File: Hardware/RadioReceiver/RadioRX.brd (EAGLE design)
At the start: 100 x 80 mm, 49 parts, among them IC1 7805TV, Q1 BSS123, Q10 BSS123, Q11 BSS123, Q12 BSS123, Q13 BSS123, Q14 BSS123, Q2 BSS123, Q3 BSS84, Q4 BSS84, Q5 BSS84, Q6 BSS84, Q7 BSS123, Q8 BSS123, Q9 BSS123

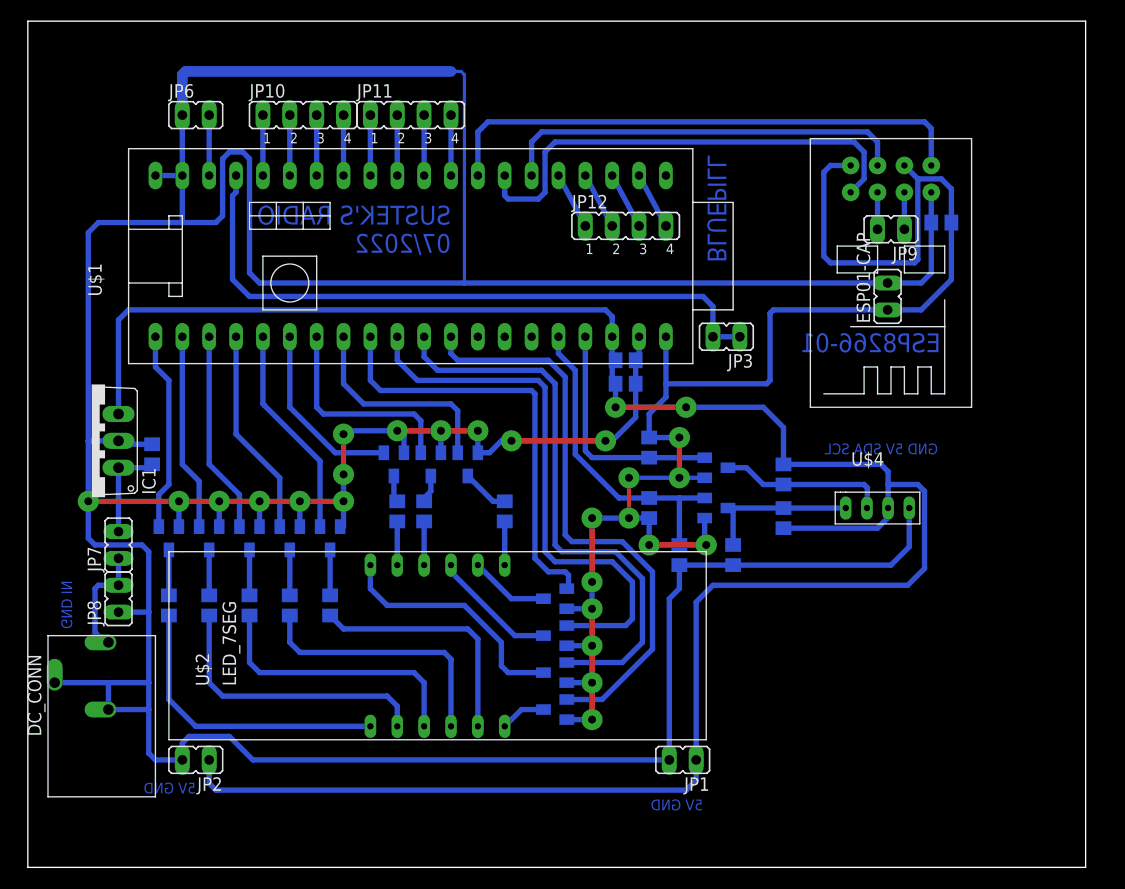
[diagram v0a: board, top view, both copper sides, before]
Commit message: Cleaned HW, prepared for NCODER, time (slows 1minute/hours)
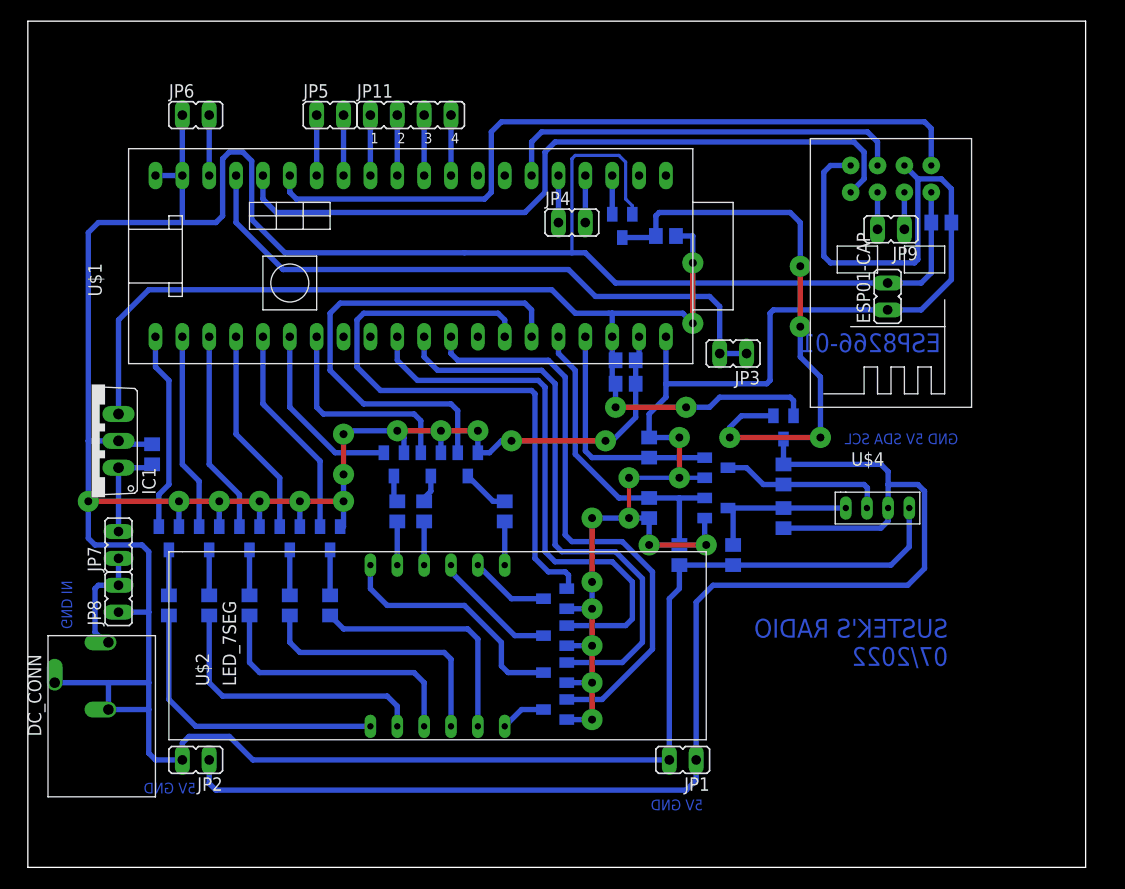
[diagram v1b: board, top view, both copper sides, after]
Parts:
- removed JP10, JP12: (no value), jumper:JP4
- added JP4, JP5: (no value), jumper:JP1
- added Q15: BSS123, transistor-small-signal:SOT23
- added Q17: BSS84, transistor-small-signal:SOT23
- added R13: 10k, rcl:R0805
- moved JP3 1.71 mm to (66.7, 48.6)
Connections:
- net N$10 renamed EE_NCS
- net N$7 renamed EE_MOSI
- net N$8 renamed EE_MISO
- net N$9 renamed EE_SCK
- removed net N$13: JP12.3, U$1.P$23
- removed net N$14: JP12.4, U$1.P$22
- removed net N$3: JP10.1, U$1.P$36
- removed net N$4: JP10.2, U$1.P$35
- removed net N$5: JP10.3, U$1.P$34
- removed net N$6: JP10.4, U$1.P$33
- new net 5V_S: JP1.1, JP2.1, Q17.3, R3.2, R4.2, U$4.P$3
- new net EE_GND: JP5.1, U$1.P$34
- new net EE_VCC: JP5.2, U$1.P$33
- new net N$15: Q15.3, Q17.1, R13.1
- new net RDA_SWITCH_PWR: Q15.1, U$1.P$23
- net 5V: now also Q17.2, R13.2; no longer JP1.1, JP2.1, R3.2, R4.2, U$4.P$3
- net ESP-RX: now also U$1.P$36; no longer U$1.P$27
- net ESP-TX: now also U$1.P$35; no longer U$1.P$28
- net GND: now also Q15.2
- net LEDC_A3: now also U$1.P$14; no longer U$1.P$9
- net LEDC_B: now also U$1.P$15; no longer U$1.P$8
- net N$11: now also JP4.1; no longer JP12.1
- net N$12: now also JP4.2; no longer JP12.2
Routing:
- net 5V_S: track 0.00 -> 127.1 mm
- net 5V: track 210.0 -> 103.8 mm, vias 2 -> 4
- net N$15: track 0.00 -> 54.6 mm, vias 0 -> 4
- net GND: track 430.4 -> 396.4 mm
- net LEDC_B: track 20.3 -> 45.3 mm
- net ESP-RX: track 45.2 -> 69.3 mm
- net ESP-TX: track 51.1 -> 72.6 mm
- net LEDC_A3: track 40.9 -> 59.1 mm
- net N$6: track 5.72 -> 0.00 mm
- net N$5: track 5.72 -> 0.00 mm
- net N$4: track 5.72 -> 0.00 mm
- net N$3: track 5.72 -> 0.00 mm
- net EE_VCC: track 0.00 -> 5.72 mm
- net EE_GND: track 0.00 -> 5.72 mm
- net N$14: track 5.40 -> 0.00 mm
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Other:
- board text removed: "BLUEPILL"

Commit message: Almost final state, just a 32.768 XTAL misses to be soldered
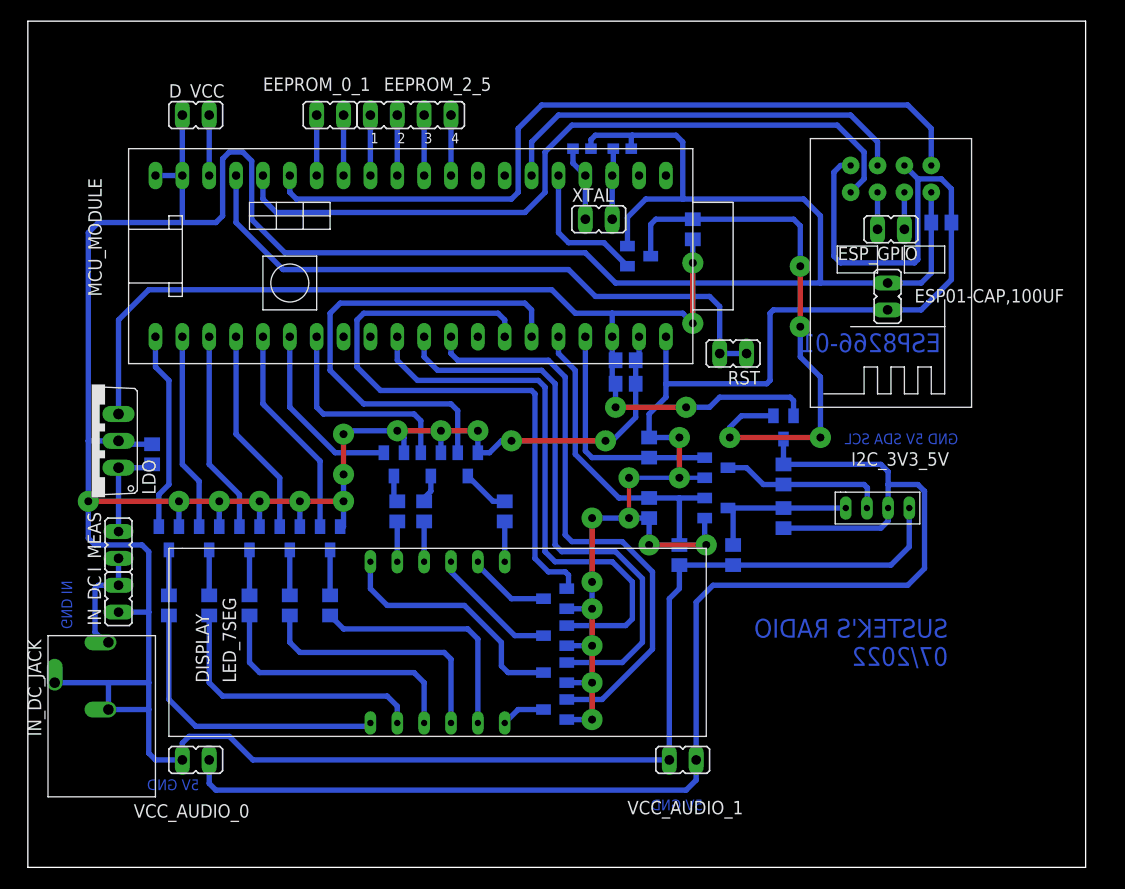
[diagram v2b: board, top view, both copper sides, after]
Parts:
- removed JP4: (no value), jumper:JP1
- removed U$2: LED_7SEG, VladimirSustek:LED_7SEG
- added C7, C8: 12p, rcl:C0603
- added DISPLAY: LED_7SEG, VladimirSustek:LED_7SEG
- added XTAL: (no value), jumper:JP1
- C1, C2: value (none) -> DNI 100p
- C3, C5, C6: value (none) -> 100n
- C4: value (none) -> 10n
- R10, R11, R12, R5, R6, R7, R8, R9: value (none) -> 220R
- moved Q13 25.7 mm to (38.1, 38.1)
- moved Q11 14.8 mm to (28.6, 31.1)
- moved Q9 3.81 mm to (21.0, 31.1)
- moved Q10 3.81 mm to (24.8, 31.1)
- moved Q7 3.81 mm to (13.3, 31.1)
- moved Q8 3.81 mm to (17.1, 31.1)
- moved Q12 3.49 mm to (41.6, 38.1)
- moved Q15 3.27 mm to (57.8, 57.8), turned to 90 degrees
- moved R13 2.62 mm to (62.9, 60.3), turned to 270 degrees
- renumbered DC_CONN to IN_DC_JACK, ESP01-CAP to ESP01-CAP,100UF, IC1 to LDO, JP1 to VCC_AUDIO_1, JP11 to EEPROM_2_5, JP2 to VCC_AUDIO_0, JP3 to RST, JP5 to EEPROM_0_1, JP6 to D_VCC, JP7 to I_MEAS, JP8 to IN_DC, JP9 to ESP_GPIO, U$1 to MCU_MODULE, U$3 to WIFI, U$4 to I2C_3V3_5V
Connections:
- removed net N$11: JP4.1, MCU_MODULE.P$25
- removed net N$12: JP4.2, MCU_MODULE.P$24
- new net GREEN_LED: MCU_MODULE.P$22
- new net N$3: C8.2, MCU_MODULE.P$23, XTAL.2
- new net N$4: C7.2, MCU_MODULE.P$24, XTAL.1
- new net NCODER_BTN: MCU_MODULE.P$28
- new net NCODER_CLK: MCU_MODULE.P$13
- new net NCODER_IN: MCU_MODULE.P$27
- new net USB_DM: MCU_MODULE.P$8
- new net USB_DP: MCU_MODULE.P$9
- net GND: now also C7.1, C8.1
- net LEDC_B: now also Q12.1; no longer Q11.1
- net LEDC_C: now also Q10.1; no longer Q9.1
- net LEDC_D: now also Q8.1; no longer Q7.1
- net LEDC_DP: now also Q9.1; no longer Q8.1
- net LEDC_E: now also Q7.1; no longer Q13.1
- net LEDC_F: now also Q13.1; no longer Q12.1
- net LEDC_G: now also Q11.1; no longer Q10.1
- net LED_A: now also DISPLAY.P$11; no longer U$2.P$11
- net LED_A1: now also DISPLAY.P$12; no longer U$2.P$12
- net LED_A2: now also DISPLAY.P$9; no longer U$2.P$9
- net LED_A3: now also DISPLAY.P$8; no longer U$2.P$8
- net LED_A4: now also DISPLAY.P$6; no longer U$2.P$6
- net LED_B: now also DISPLAY.P$7; no longer U$2.P$7
- net LED_C: now also DISPLAY.P$4; no longer U$2.P$4
- net LED_D: now also DISPLAY.P$2; no longer U$2.P$2
- net LED_DP: now also DISPLAY.P$3; no longer U$2.P$3
- net LED_E: now also DISPLAY.P$1; no longer U$2.P$1
- net LED_F: now also DISPLAY.P$10; no longer U$2.P$10
- net LED_G: now also DISPLAY.P$5; no longer U$2.P$5
- net N$18: now also Q7.3; no longer Q13.3
- net N$19: now also Q8.3; no longer Q7.3
- net N$20: now also Q9.3; no longer Q8.3
- net N$21: now also Q10.3; no longer Q9.3
- net N$22: now also Q11.3; no longer Q10.3
- net N$23: now also Q12.3; no longer Q11.3
- net N$24: now also Q13.3; no longer Q12.3
- net RDA_SWITCH_PWR: now also MCU_MODULE.P$25; no longer MCU_MODULE.P$23
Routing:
- net GND: track 396.4 -> 422.2 mm
- net RDA_SWITCH_PWR: track 3.67 -> 13.2 mm
- net N$4: track 0.00 -> 7.15 mm
- net N$3: track 0.00 -> 6.71 mm
- net N$12: track 4.45 -> 0.00 mm
- net N$11: track 4.45 -> 0.00 mm
- net N$15: track 54.6 -> 52.5 mm
- net 5V: track 103.8 -> 101.9 mm
- net 3V3: track 148.8 -> 146.9 mm
- net ESP-TX: track 72.6 -> 74.1 mm
- net ESP-RX: track 69.3 -> 70.6 mm
- net ESP-RST: track 38.9 -> 40.2 mm
